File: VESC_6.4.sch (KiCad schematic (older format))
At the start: 23 parts, among them J1 CAN, J2 HALL_ENC, J3 COMM, J4 SERVO, J5 SWD, J6 USB_OTG, SW1 SENSOR_VOLTAGE

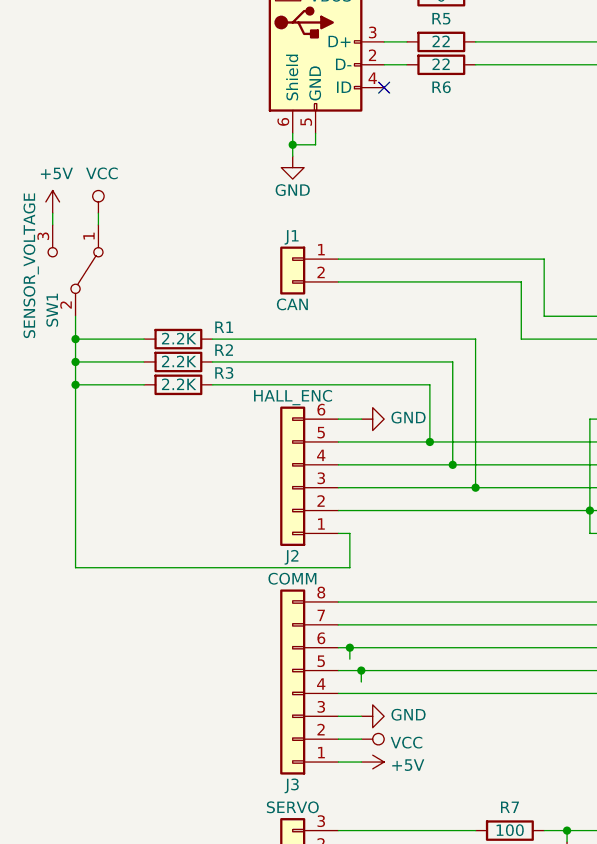
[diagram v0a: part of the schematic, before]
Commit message: removed HALL switch, added bulk capacitor, updated sheet's datestamp
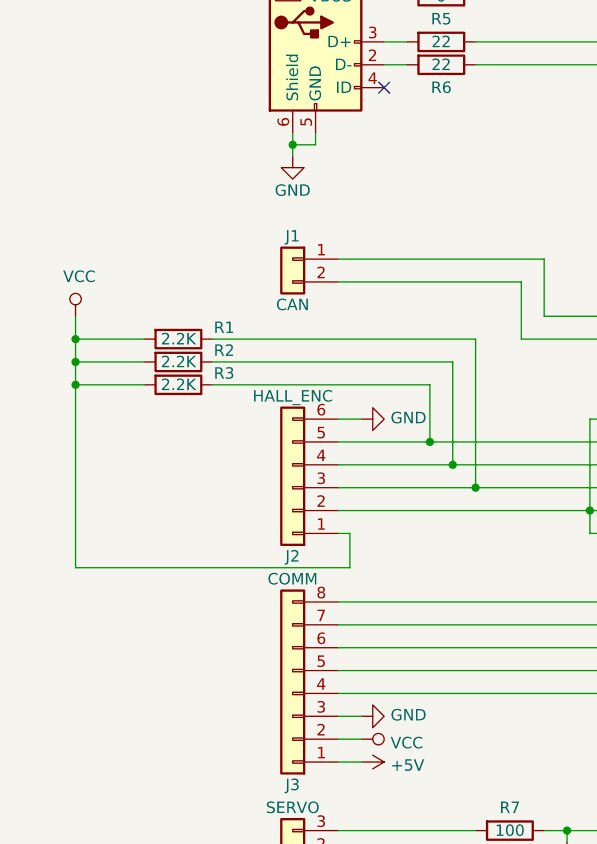
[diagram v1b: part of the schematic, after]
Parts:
- removed SW1: SENSOR_VOLTAGE, Global_Parts:JS102011JCQN, symbol SW_SPDT
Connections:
- net VCC: now also J2.1 (Pin_1), R1.2, R2.2, R3.2
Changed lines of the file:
@@
 Sheet 1 5
 Title "VESC 6.4 "
-Date "2018-02-05"
+Date "2018-05-04"
 Rev "1a"
 Comp ""
@@
 $EndComp
 $Comp
-L SW_SPDT SW1
-U 1 1 5A79C7B9
-P 1350 2300
-F 0 "SW1" H 1100 2200 50  0000 L CNN
-F 1 "SENSOR_VOLTAGE" H 1050 2100 50  0000 L CNN
-F 2 "Global_Parts:JS102011JCQN" H 1350 2300 50  0001 C CNN
-F 3 "" H 1350 2300 50  0001 C CNN
-	1    1350 2300
-	0    1    -1   0
-$EndComp
-$Comp
 L VCC #PWR02
 U 1 1 5A79CD83
-P 1450 2050
-F 0 "#PWR02" H 1450 1900 50  0001 C CNN
-F 1 "VCC" H 1467 2223 50  0000 C CNN
-F 2 "" H 1450 2050 50  0001 C CNN
-F 3 "" H 1450 2050 50  0001 C CNN
-	1    1450 2050
-	1    0    0    -1
-$EndComp
-$Comp
-L +5V #PWR01
-U 1 1 5A79D04F
-P 1250 2050
-F 0 "#PWR01" H 1250 1900 50  0001 C CNN
-F 1 "+5V" H 1265 2223 50  0000 C CNN
-F 2 "" H 1250 2050 50  0001 C CNN
-F 3 "" H 1250 2050 50  0001 C CNN
-	1    1250 2050
+P 1350 2500
+F 0 "#PWR02" H 1350 2350 50  0001 C CNN
+F 1 "VCC" H 1367 2673 50  0000 C CNN
+F 2 "" H 1350 2500 50  0001 C CNN
+F 3 "" H 1350 2500 50  0001 C CNN
+	1    1350 2500
 	1    0    0    -1
 $EndComp
@@
 Connection ~ 1350 2800
 Wire Wire Line
-	1450 2050 1450 2100
-Wire Wire Line
-	1250 2050 1250 2100
-Wire Wire Line
 	4300 2600 4400 2600
 Wire Wire Line
@@
 	8900 2300 8400 2300
 Wire Wire Line
-	2550 4000 2550 3950
-Connection ~ 2550 3950
-Wire Wire Line
-	2600 4100 2600 4050
-Connection ~ 2600 4050
-Wire Wire Line
 	8900 1800 8400 1800
